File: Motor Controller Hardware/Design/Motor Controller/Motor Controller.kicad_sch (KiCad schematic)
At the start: 10 parts, among them J1 Phase U L, J2 Phase U H, J3 Phase V L, J4 Phase V H, J5 Phase W L, J6 Phase W H

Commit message: A
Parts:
- J1, J2, J3, J4, J5, J6: footprint Connector_PinHeader_2.54mm:PinHeader_1x03_P2.54mm_Vertical -> Connector_PinHeader_1.27mm:PinHeader_1x03_P1.27mm_Vertical
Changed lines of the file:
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@@
 			)
 		)
-		(property "Footprint" "Connector_PinHeader_2.54mm:PinHeader_1x03_P2.54mm_Vertical"
+		(property "Footprint" "Connector_PinHeader_1.27mm:PinHeader_1x03_P1.27mm_Vertical"
 			(at 254 133.35 0)
 			(effects
@@
 			)
 		)
-		(property "Footprint" "Connector_PinHeader_2.54mm:PinHeader_1x03_P2.54mm_Vertical"
+		(property "Footprint" "Connector_PinHeader_1.27mm:PinHeader_1x03_P1.27mm_Vertical"
 			(at 254 142.24 0)
 			(effects
@@
 			)
 		)
-		(property "Footprint" "Connector_PinHeader_2.54mm:PinHeader_1x03_P2.54mm_Vertical"
+		(property "Footprint" "Connector_PinHeader_1.27mm:PinHeader_1x03_P1.27mm_Vertical"
 			(at 254 115.57 0)
 			(effects
@@
 			)
 		)
-		(property "Footprint" "Connector_PinHeader_2.54mm:PinHeader_1x03_P2.54mm_Vertical"
+		(property "Footprint" "Connector_PinHeader_1.27mm:PinHeader_1x03_P1.27mm_Vertical"
 			(at 254 151.13 0)
 			(effects
@@
 			)
 		)
-		(property "Footprint" "Connector_PinHeader_2.54mm:PinHeader_1x03_P2.54mm_Vertical"
+		(property "Footprint" "Connector_PinHeader_1.27mm:PinHeader_1x03_P1.27mm_Vertical"
 			(at 254 124.46 0)
 			(effects
@@
 			)
 		)
-		(property "Footprint" "Connector_PinHeader_2.54mm:PinHeader_1x03_P2.54mm_Vertical"
+		(property "Footprint" "Connector_PinHeader_1.27mm:PinHeader_1x03_P1.27mm_Vertical"
 			(at 254 106.68 0)
 			(effects

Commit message: A
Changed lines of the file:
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@@
 	(wire
 		(pts
-			(xy 193.04 38.1) (xy 190.5 38.1)
+			(xy 193.04 25.4) (xy 190.5 25.4)
 		)
 		(stroke
@@
 	(wire
 		(pts
-			(xy 193.04 35.56) (xy 190.5 35.56)
+			(xy 193.04 22.86) (xy 190.5 22.86)
 		)
 		(stroke
@@
 	(wire
 		(pts
-			(xy 193.04 30.48) (xy 190.5 30.48)
+			(xy 193.04 17.78) (xy 190.5 17.78)
 		)
 		(stroke
@@
 	(wire
 		(pts
-			(xy 193.04 40.64) (xy 190.5 40.64)
+			(xy 193.04 27.94) (xy 190.5 27.94)
 		)
 		(stroke
@@
 	)
 	(label "DRV_EN"
-		(at 193.04 40.64 0)
+		(at 193.04 27.94 0)
 		(fields_autoplaced yes)
 		(effects
@@
 	)
 	(label "EXT_NRST_Controller_A"
-		(at 193.04 38.1 0)
+		(at 193.04 25.4 0)
 		(fields_autoplaced yes)
 		(effects
@@
 	)
 	(label "GATE_DRIVER_FAULT_OUT"
-		(at 193.04 35.56 0)
+		(at 193.04 22.86 0)
 		(fields_autoplaced yes)
 		(effects
@@
 	)
 	(label "EXT_NRST_Controller_B_IN"
-		(at 193.04 30.48 0)
+		(at 193.04 17.78 0)
 		(fields_autoplaced yes)
 		(effects
@@
 	)
 	(sheet
-		(at 160.02 25.4)
-		(size 30.48 17.78)
+		(at 160.02 15.24)
+		(size 30.48 38.1)
 		(fields_autoplaced yes)
 		(stroke
@@
 		)
 		(property "Sheetname" "Isolated Driver Interface"
-			(at 160.02 24.6884 0)
+			(at 160.02 14.5284 0)
 			(effects
 				(font
@@
 		)
 		(property "Sheetfile" "Isolated_Driver_Interface.kicad_sch"
-			(at 160.02 44.3996 0)
+			(at 160.02 53.9246 0)
 			(effects
 				(font
@@
 		)
 		(pin "EXT_NRST_Controller_A_IN" input
-			(at 190.5 38.1 0)
+			(at 190.5 25.4 0)
 			(effects
 				(font
@@
 		)
 		(pin "EXT_DRV_EN_IN" input
-			(at 190.5 40.64 0)
+			(at 190.5 27.94 0)
 			(effects
 				(font
@@
 		)
 		(pin "EXT_POWER_STAGE_EN_IN" input
-			(at 190.5 33.02 0)
+			(at 190.5 20.32 0)
 			(effects
 				(font
@@
 		)
 		(pin "GATE_DRIVER_FAULT_OUT" input
-			(at 190.5 35.56 0)
+			(at 190.5 22.86 0)
 			(effects
 				(font
@@
 		)
 		(pin "EXT_NRST_Controller_B_IN" input
-			(at 190.5 30.48 0)
+			(at 190.5 17.78 0)
 			(effects
 				(font

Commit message: A:
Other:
- sheet Position Sensing ports: added HALL_U, HALL_W; removed HALL_UX, HALL_WY
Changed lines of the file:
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@@
 			)
 		)
-		(pin "HALL_UX" input
-			(at 187.96 68.58 180)
+		(pin "HALL_V" input
+			(at 187.96 66.04 180)
 			(effects
 				(font
@@
 			)
 		)
-		(pin "HALL_WY" input
+		(pin "HALL_W" input
 			(at 187.96 63.5 180)
 			(effects
@@
 			)
 		)
-		(pin "HALL_V" input
-			(at 187.96 66.04 180)
+		(pin "HALL_U" input
+			(at 187.96 68.58 180)
 			(effects
 				(font

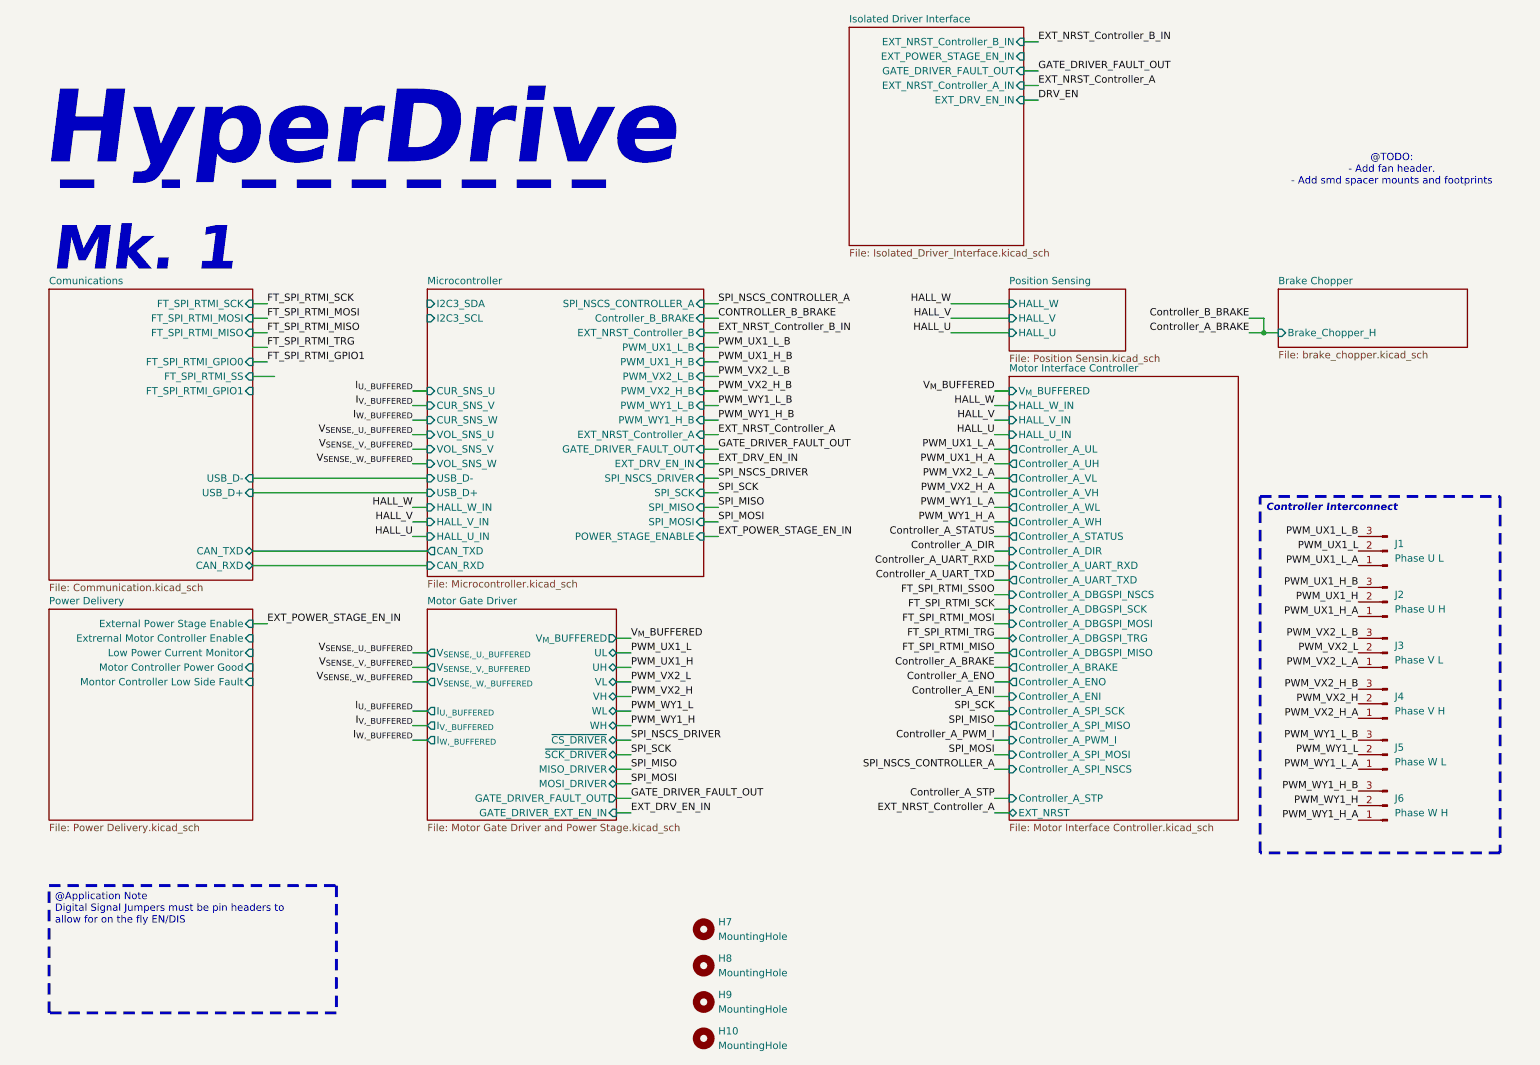
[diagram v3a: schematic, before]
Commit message: Changed size to 120x100 and routing 90%
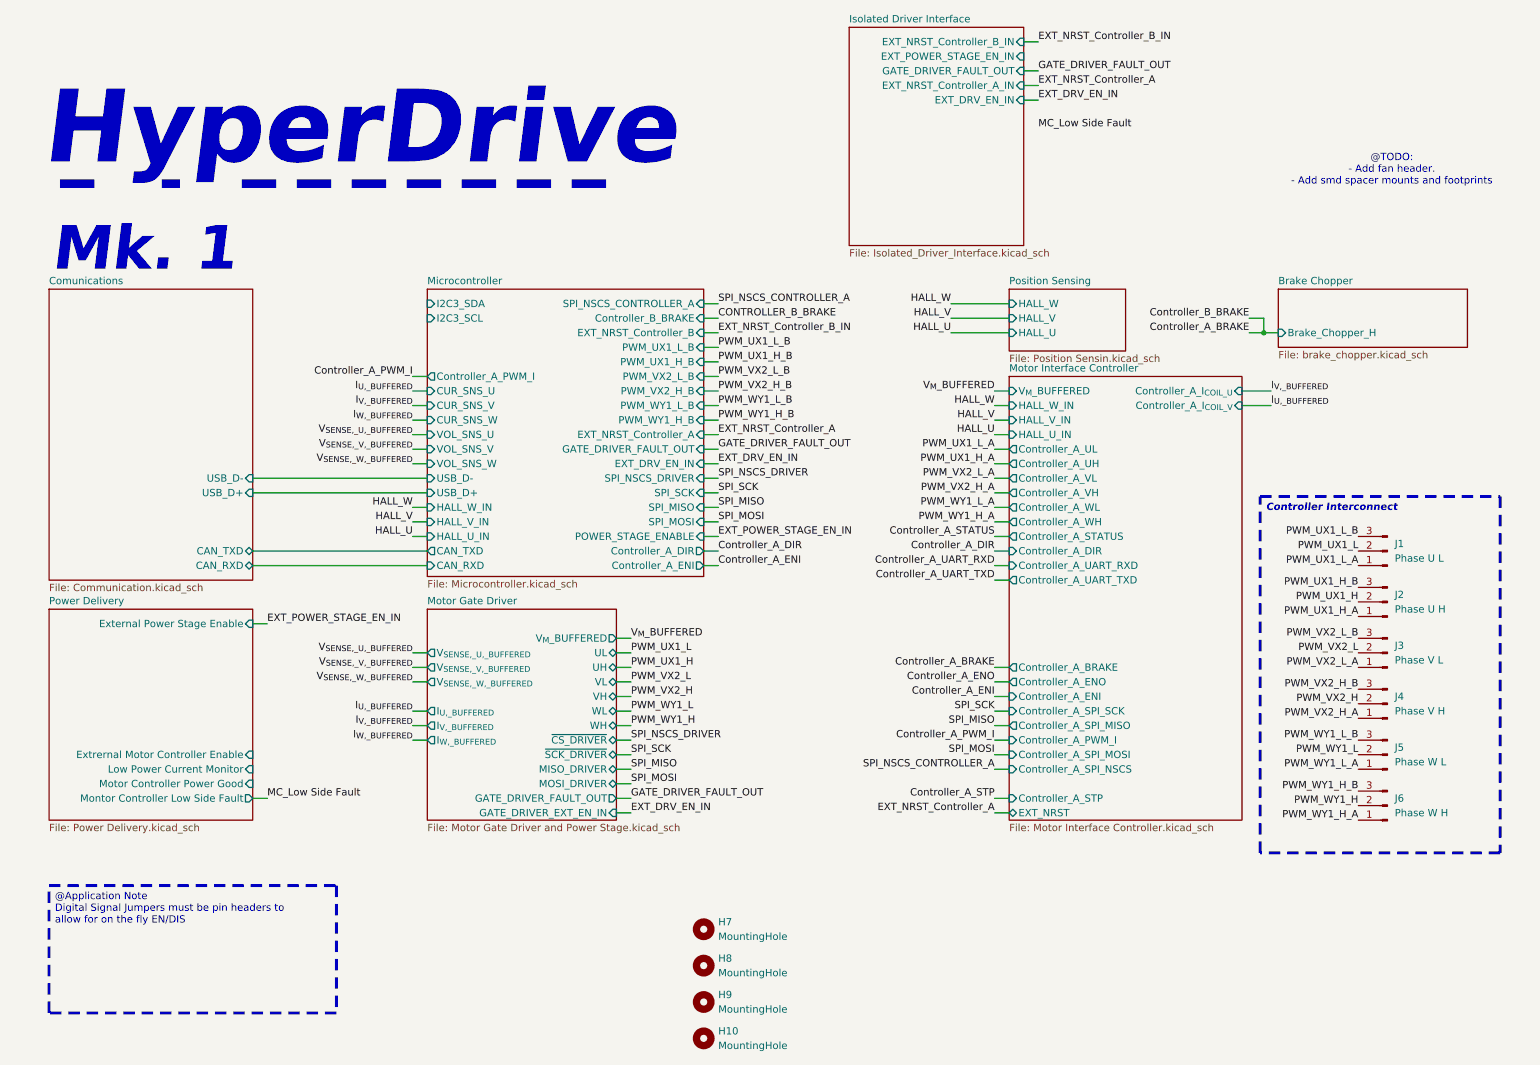
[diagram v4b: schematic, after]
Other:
- sheet Comunications ports: added none; removed FT_SPI_RTMI_GPIO0, FT_SPI_RTMI_GPIO1, FT_SPI_RTMI_MISO, FT_SPI_RTMI_MOSI, FT_SPI_RTMI_SCK, FT_SPI_RTMI_SS
- sheet Microcontroller ports: added Controller_A_DIR, Controller_A_ENI, Controller_A_PWM_I; removed none
- sheet Motor Interface Controller ports: added Controller_A_I_{COIL_U}, Controller_A_I_{COIL_V}; removed Controller_A_DBGSPI_MISO, Controller_A_DBGSPI_MOSI, Controller_A_DBGSPI_NSCS, Controller_A_DBGSPI_SCK, Controller_A_DBGSPI_TRG

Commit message: A
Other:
- removed sheet Brake Chopper
- sheet Isolated Driver Interface ports: added none; removed EXT_POWER_STAGE_EN_IN
- sheet Microcontroller ports: added CUR_SNS_LOW_SIDE, EXT_DRV_EN_MCU_OUT, GATE_DRIVER_FAULT_IN, PWM_U_H_B, PWM_U_L_B, PWM_V_H_B, PWM_V_L_B, PWM_W_H_B, PWM_W_L_B; removed EXT_DRV_EN_IN, GATE_DRIVER_FAULT_OUT, PWM_UX1_H_B, PWM_UX1_L_B, PWM_VX2_H_B, PWM_VX2_L_B, PWM_WY1_H_B, PWM_WY1_L_B
- sheet Motor Gate Driver ports: added SCK_DRIVER; removed ~{SCK_DRIVER}
- sheet Motor Interface Controller ports: added none; removed Controller_A_STP, Controller_A_UART_RXD, Controller_A_UART_TXD
- sheet Power Delivery ports: added none; removed Extrernal Motor Controller Enable, Montor Controller Low Side Fault, Motor Controller Power Good

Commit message: A
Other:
- sheet Microcontroller ports: added none; removed I2C3_SCL, I2C3_SDA
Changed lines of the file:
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@@
-			)
-		)
-		(pin "I2C3_SDA" input
-			(at 86.36 63.5 180)
-			(effects
-				(font
-					(size 1.27 1.27)
-				)
-				(justify left)
-			)
-		)
-		(pin "I2C3_SCL" input
-			(at 86.36 66.04 180)
-			(effects
-				(font
-					(size 1.27 1.27)
-				)
-				(justify left)
 			)
 		)

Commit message: A
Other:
- sheet Comunications ports: added CAN_RXD_ISO, CAN_TXD_ISO; removed CAN_RXD, CAN_TXD
- sheet Isolated Driver Interface ports: added ANALOG_SPEED_IN, CONTROLLER_STATUS_OUT; removed none
- sheet Microcontroller ports: added ANALOG_SPEED_IN, CONTROLLER_A_STATUS_IN, CONTROLLER_B_STATUS_OUT; removed Controller_B_BRAKE, EXT_NRST_Controller_A
- sheet Motor Interface Controller ports: added none; removed Controller_A_BRAKE, Controller_A_ENO
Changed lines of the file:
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@@
 	(wire
 		(pts
+			(xy 83.82 71.12) (xy 86.36 71.12)
+		)
+		(stroke
+			(width 0)
+			(type default)
+		)
+	)
+	(wire
+		(pts
 			(xy 134.62 71.12) (xy 137.16 71.12)
 		)
@@
 	(wire
 		(pts
+			(xy 50.8 160.02) (xy 53.34 160.02)
+		)
+		(stroke
+			(width 0)
+			(type default)
+		)
+	)
+	(wire
+		(pts
 			(xy 134.62 91.44) (xy 137.16 91.44)
 		)
@@
 	(wire
 		(pts
-			(xy 185.42 129.54) (xy 187.96 129.54)
-		)
-		(stroke
-			(width 0)
-			(type default)
-		)
-	)
-	(wire
-		(pts
 			(xy 119.38 152.4) (xy 121.92 152.4)
 		)
@@
 	(wire
 		(pts
-			(xy 134.62 66.04) (xy 137.16 66.04)
+			(xy 134.62 93.98) (xy 137.16 93.98)
 		)
 		(stroke
@@
 	(wire
 		(pts
-			(xy 134.62 93.98) (xy 137.16 93.98)
+			(xy 185.42 137.16) (xy 187.96 137.16)
 		)
 		(stroke
@@
 	(wire
 		(pts
-			(xy 185.42 137.16) (xy 187.96 137.16)
+			(xy 185.42 96.52) (xy 187.96 96.52)
 		)
 		(stroke
@@
 	(wire
 		(pts
-			(xy 185.42 96.52) (xy 187.96 96.52)
+			(xy 228.6 81.28) (xy 233.68 81.28)
 		)
 		(stroke
@@
 	(wire
 		(pts
-			(xy 228.6 81.28) (xy 233.68 81.28)
+			(xy 83.82 134.62) (xy 86.36 134.62)
 		)
 		(stroke
@@
 	(wire
 		(pts
-			(xy 83.82 134.62) (xy 86.36 134.62)
+			(xy 83.82 139.7) (xy 86.36 139.7)
 		)
 		(stroke
@@
 	(wire
 		(pts
-			(xy 83.82 139.7) (xy 86.36 139.7)
+			(xy 134.62 73.66) (xy 137.16 73.66)
 		)
 		(stroke
@@
 	(wire
 		(pts
-			(xy 134.62 73.66) (xy 137.16 73.66)
+			(xy 50.8 163.83) (xy 53.34 163.83)
 		)
 		(stroke
@@
 	(wire
 		(pts
-			(xy 185.42 127) (xy 187.96 127)
-		)
-		(stroke
-			(width 0)
-			(type default)
-		)
-	)
-	(wire
-		(pts
 			(xy 119.38 139.7) (xy 121.92 139.7)
 		)
@@
 	(wire
 		(pts
-			(xy 134.62 86.36) (xy 137.16 86.36)
+			(xy 55.88 93.98) (xy 86.36 93.98)
 		)
 		(stroke
@@
 	(wire
 		(pts
-			(xy 55.88 93.98) (xy 86.36 93.98)
+			(xy 83.82 63.5) (xy 86.36 63.5)
+		)
+		(stroke
+			(width 0)
+			(type default)
+		)
+	)
+	(wire
+		(pts
+			(xy 83.82 66.04) (xy 86.36 66.04)
 		)
 		(stroke
@@
 		)
 	)
-	(label "Controller_A_ENO"
-		(at 185.42 129.54 180)
-		(fields_autoplaced yes)
-		(effects
-			(font
-				(size 1.27 1.27)
-			)
-			(justify right bottom)
-		)
-	)
 	(label "I_{W,_BUFFERED}"
 		(at 83.82 83.82 180)
@@
 		)
 	)
+	(label "Controller_B_ANALOG_SPEED"
+		(at 53.34 163.83 0)
+		(fields_autoplaced yes)
+		(effects
+			(font
+				(size 1.27 1.27)
+			)
+			(justify left bottom)
+		)
+	)
 	(label "Controller_A_DIR"
 		(at 185.42 106.68 180)
@@
 		)
 	)
+	(label "Controller_B_STATUS"
+		(at 83.82 71.12 180)
+		(fields_autoplaced yes)
+		(effects
+			(font
+				(size 1.27 1.27)
+			)
+			(justify right bottom)
+		)
+	)
 	(label "Low Power Current Monitor"
 		(at 83.82 73.66 180)
@@
 		)
 	)
+	(label "Controller_A_STATUS"
+		(at 83.82 66.04 180)
+		(fields_autoplaced yes)
+		(effects
+			(font
+				(size 1.27 1.27)
+			)
+			(justify right bottom)
+		)
+	)
 	(label "SPI_NSCS_DRIVER"
 		(at 121.92 139.7 0)
@@
 		)
 	)
-	(label "CONTROLLER_B_BRAKE"
-		(at 137.16 66.04 0)
-		(fields_autoplaced yes)
-		(effects
-			(font
-				(size 1.27 1.27)
-			)
-			(justify left bottom)
-		)
-	)
 	(label "Controller_A_ENI"
 		(at 185.42 132.08 180)
@@
 		)
 	)
-	(label "EXT_NRST_Controller_A"
-		(at 137.16 86.36 0)
-		(fields_autoplaced yes)
-		(effects
-			(font
-				(size 1.27 1.27)
-			)
-			(justify left bottom)
-		)
-	)
 	(label "PWM_VX2_L"
 		(at 248.92 124.46 180)
@@
 		)
 	)
-	(label "Controller_A_BRAKE"
-		(at 185.42 127 180)
-		(fields_autoplaced yes)
-		(effects
-			(font
-				(size 1.27 1.27)
-			)
-			(justify right bottom)
-		)
-	)
 	(label "V_{SENSE,_W,_BUFFERED}"
 		(at 83.82 91.44 180)
@@
 		)
 	)
+	(label "Controller_B_STATUS"
+		(at 53.34 160.02 0)
+		(fields_autoplaced yes)
+		(effects
+			(font
+				(size 1.27 1.27)
+			)
+			(justify left bottom)
+		)
+	)
 	(label "SPI_SCK"
 		(at 137.16 96.52 0)
@@
 		)
 	)
+	(label "Controller_B_ANALOG_SPEED"
+		(at 83.82 63.5 180)
+		(fields_autoplaced yes)
+		(effects
+			(font
+				(size 1.27 1.27)
+			)
+			(justify right bottom)
+		)
+	)
 	(label "PWM_WY1_H"
 		(at 248.92 151.13 180)
@@
 			)
 		)
-		(pin "Controller_A_BRAKE" output
-			(at 187.96 127 180)
-			(effects
-				(font
-					(size 1.27 1.27)
-				)
-				(justify left)
-			)
-		)
-		(pin "Controller_A_ENO" output
-			(at 187.96 129.54 180)
-			(effects
-				(font
-					(size 1.27 1.27)
-				)
-				(justify left)
-			)
-		)
 		(pin "Controller_A_ENI" input
 			(at 187.96 132.08 180)
@@
 			)
 		)
+		(pin "CONTROLLER_STATUS_OUT" input
+			(at 50.8 160.02 0)
+			(effects
+				(font
+					(size 1.27 1.27)
+				)
+				(justify right)
+			)
+		)
+		(pin "ANALOG_SPEED_IN" input
+			(at 50.8 163.83 0)
+			(effects
+				(font
+					(size 1.27 1.27)
+				)
+				(justify right)
+			)
+		)
 		(instances
 			(project "Motor Controller"
@@
 			)
 		)
-		(pin "Controller_B_BRAKE" input
-			(at 134.62 66.04 0)
-			(effects
-				(font
-					(size 1.27 1.27)
-				)
-				(justify right)
-			)
-		)
 		(pin "EXT_NRST_Controller_B" input
 			(at 134.62 68.58 0)
@@
 			)
 		)
-		(pin "EXT_NRST_Controller_A" input
-			(at 134.62 86.36 0)
+		(pin "CONTROLLER_A_STATUS_IN" input
+			(at 86.36 66.04 180)
 			(effects
 				(font
 					(size 1.27 1.27)
 				)
-				(justify right)
+				(justify left)
+			)
+		)
+		(pin "CONTROLLER_B_STATUS_OUT" output
+			(at 86.36 71.12 180)
+			(effects
+				(font
+					(size 1.27 1.27)
+				)
+				(justify left)
+			)
+		)
+		(pin "ANALOG_SPEED_IN" input
+			(at 86.36 63.5 180)
+			(effects
+				(font
+					(size 1.27 1.27)
+				)
+				(justify left)
 			)
 		)
@@
 	)
 	(sheet
-		(at 20.32 60.96)
-		(size 35.56 50.8)
+		(at 20.32 91.44)
+		(size 35.56 20.32)
 		(fields_autoplaced yes)
 		(stroke
@@
 		)
 		(property "Sheetname" "Comunications"
-			(at 20.32 60.2484 0)
+			(at 20.32 90.7284 0)
 			(effects
 				(font
@@
 		)
 		(property "Field2" ""
-			(at 20.32 60.96 0)
+			(at 20.32 91.44 0)
 			(effects
 				(font
@@
 			)
 		)
-		(pin "CAN_TXD" bidirectional
-			(at 55.88 106.68 0)
+		(pin "USB_D-" input
+			(at 55.88 93.98 0)
 			(effects
 				(font
@@
 			)
 		)
-		(pin "CAN_RXD" bidirectional
-			(at 55.88 109.22 0)
+		(pin "USB_D+" input
+			(at 55.88 96.52 0)
 			(effects
 				(font
@@
 			)
 		)
-		(pin "USB_D-" input
-			(at 55.88 93.98 0)
+		(pin "CAN_TXD_ISO" bidirectional
+			(at 55.88 106.68 0)
 			(effects
 				(font
@@
 			)
 		)
-		(pin "USB_D+" input
-			(at 55.88 96.52 0)
+		(pin "CAN_RXD_ISO" bidirectional
+			(at 55.88 109.22 0)
 			(effects
 				(font

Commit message: A
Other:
- sheet Isolated Driver Interface ports: added EXT_NRST_Controllers; removed EXT_NRST_Controller_A_IN, EXT_NRST_Controller_B_IN
- sheet Microcontroller ports: added Controller_A_RESET_OUT; removed none
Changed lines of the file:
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@@
-	(wire
-		(pts
-			(xy 53.34 146.05) (xy 50.8 146.05)
-		)
-		(stroke
-			(width 0)
-			(type default)
-		)
-	)
 	(wire
 		(pts
@@
 		(pts
 			(xy 83.82 83.82) (xy 86.36 83.82)
+		)
+		(stroke
+			(width 0)
+			(type default)
+		)
+	)
+	(wire
+		(pts
+			(xy 83.82 68.58) (xy 86.36 68.58)
 		)
 		(stroke
@@
 		)
 	)
+	(label "EXT_NRST_Controllers"
+		(at 137.16 68.58 0)
+		(fields_autoplaced yes)
+		(effects
+			(font
+				(size 1.27 1.27)
+			)
+			(justify left bottom)
+		)
+	)
 	(label "I_{W,_BUFFERED}"
 		(at 83.82 83.82 180)
@@
 		)
 	)
+	(label "EXT_NRST_Controllers"
+		(at 83.82 68.58 180)
+		(fields_autoplaced yes)
+		(effects
+			(font
+				(size 1.27 1.27)
+			)
+			(justify right bottom)
+		)
+	)
 	(label "PWM_VX2_L_A"
 		(at 185.42 93.98 180)
@@
 		)
 	)
-	(label "EXT_NRST_Controller_A"
+	(label "EXT_NRST_Controllers"
 		(at 53.34 153.67 0)
 		(fields_autoplaced yes)
@@
 		)
 	)
-	(label "EXT_NRST_Controller_A"
+	(label "EXT_NRST_Controllers"
 		(at 185.42 152.4 180)
 		(fields_autoplaced yes)
@@
 		)
 	)
-	(label "EXT_NRST_Controller_B_IN"
-		(at 53.34 146.05 0)
-		(fields_autoplaced yes)
-		(effects
-			(font
-				(size 1.27 1.27)
-			)
-			(justify left bottom)
-		)
-	)
 	(label "GATE_DRIVER_FAULT_OUT"
 		(at 121.92 149.86 0)
@@
 			)
 			(justify right bottom)
-		)
-	)
-	(label "EXT_NRST_Controller_B_IN"
-		(at 137.16 68.58 0)
-		(fields_autoplaced yes)
-		(effects
-			(font
-				(size 1.27 1.27)
-			)
-			(justify left bottom)
 		)
 	)
@@
 			)
 		)
-		(pin "EXT_NRST_Controller_A_IN" input
-			(at 50.8 153.67 0)
-			(effects
-				(font
-					(size 1.27 1.27)
-				)
-				(justify right)
-			)
-		)
 		(pin "EXT_DRV_EN_IN" input
 			(at 50.8 156.21 0)
@@
 			)
 		)
-		(pin "EXT_NRST_Controller_B_IN" input
-			(at 50.8 146.05 0)
-			(effects
-				(font
-					(size 1.27 1.27)
-				)
-				(justify right)
-			)
-		)
 		(pin "CONTROLLER_STATUS_OUT" input
 			(at 50.8 160.02 0)
@@
 		(pin "ANALOG_SPEED_IN" input
 			(at 50.8 163.83 0)
+			(effects
+				(font
+					(size 1.27 1.27)
+				)
+				(justify right)
+			)
+		)
+		(pin "EXT_NRST_Controllers" input
+			(at 50.8 153.67 0)
 			(effects
 				(font
@@
 			(effects
 				(font
+					(size 1.27 1.27)
+				)
+				(justify left)
+			)
+		)
+		(pin "Controller_A_RESET_OUT" output
+			(at 86.36 68.58 180)
+			(effects
+				(font
